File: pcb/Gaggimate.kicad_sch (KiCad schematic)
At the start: 66 parts, among them J1 USB_C_Receptacle, J10 Conn_01x02, J2 Conn_01x02, J3 Conn_01x03, J4 Conn_01x04, J5 Conn_01x04, J6 Conn_01x10, J7 Conn_01x02, J8 Conn_01x02, J9 Conn_01x04, K1 Relay_SPDT, K2 Relay_SPDT, K3 Relay_SPDT, Q1 MMBT2222A, Q2 MMBT2222A, Q3 MMBT2222A, SW1 SW_Push, SW2 SW_Push, U1 ESP32-S3-WROOM-1, U2 AMS1117-3.3, U3 USBLC6-2SC6, U6 MAX31855EASA

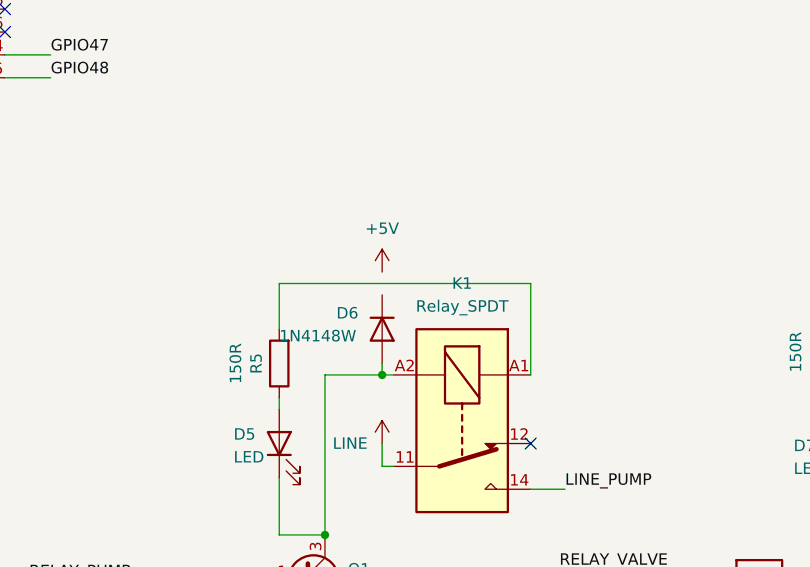
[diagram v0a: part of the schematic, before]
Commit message: feat: Add adjustments to PCB, pcb diff pipeline
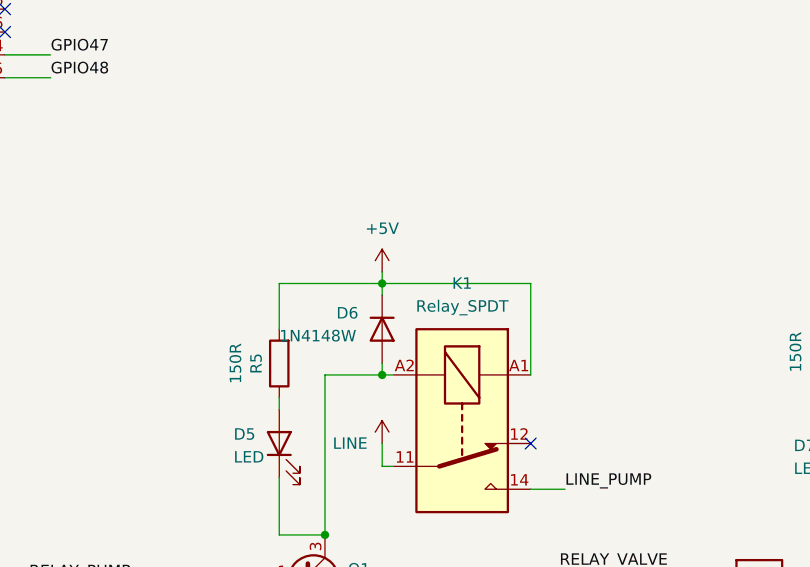
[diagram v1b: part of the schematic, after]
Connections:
- net +5V: now also D6.1 (K), K1.A1, R5.2
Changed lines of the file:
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@@
+	)
+	(junction
+		(at 240.03 135.89)
+		(diameter 0)
+		(color 0 0 0 0)
 	)
 	(junction
@@
 	(wire
 		(pts
+			(xy 240.03 134.62) (xy 240.03 135.89)
+		)
+		(stroke
+			(width 0)
+			(type default)
+		)
+	)
+	(wire
+		(pts
 			(xy 127.762 152.654) (xy 138.938 152.654)
 		)
@@
 	(wire
 		(pts
+			(xy 240.03 135.89) (xy 256.54 135.89)
+		)
+		(stroke
+			(width 0)
+			(type default)
+		)
+	)
+	(wire
+		(pts
 			(xy 358.14 92.71) (xy 361.95 92.71)
 		)
@@
 	(wire
 		(pts
-			(xy 228.6 135.89) (xy 256.54 135.89)
+			(xy 228.6 135.89) (xy 240.03 135.89)
 		)
 		(stroke
@@
 		)
 		(stroke
+			(width 0)
+			(type default)
+		)
+	)
+	(wire
+		(pts
+			(xy 240.03 135.89) (xy 240.03 137.16)
+		)
+		(stroke

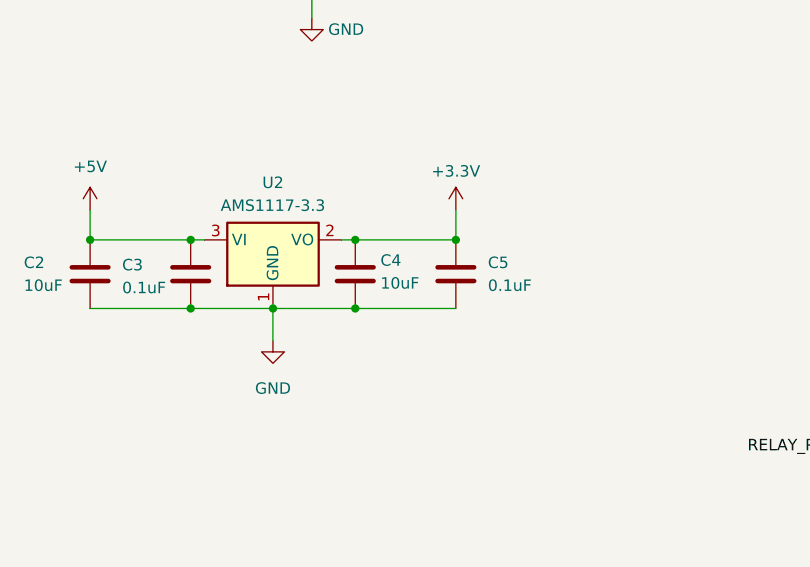
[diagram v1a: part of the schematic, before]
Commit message: feat: Replace 10uF output capacitor with 22uF
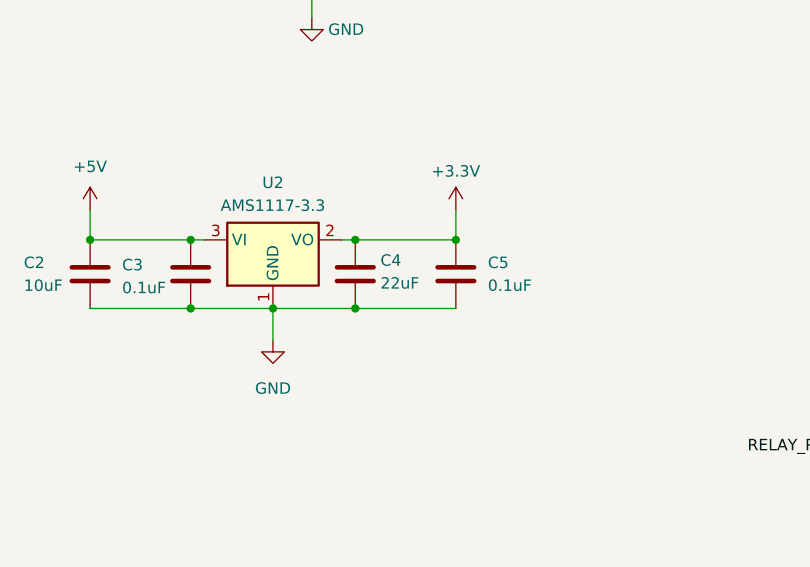
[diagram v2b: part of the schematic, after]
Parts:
- C4: value 10uF -> 22uF; LCSC C15850 -> C45783
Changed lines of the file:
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@@
 			)
 		)
-		(property "Value" "10uF"
+		(property "Value" "22uF"
 			(at 160.02 149.86 0)
 			(effects
@@
 			)
 		)
-		(property "LCSC" "C15850"
+		(property "LCSC" "C45783"
 			(at 160.02 147.32 0)
 			(effects

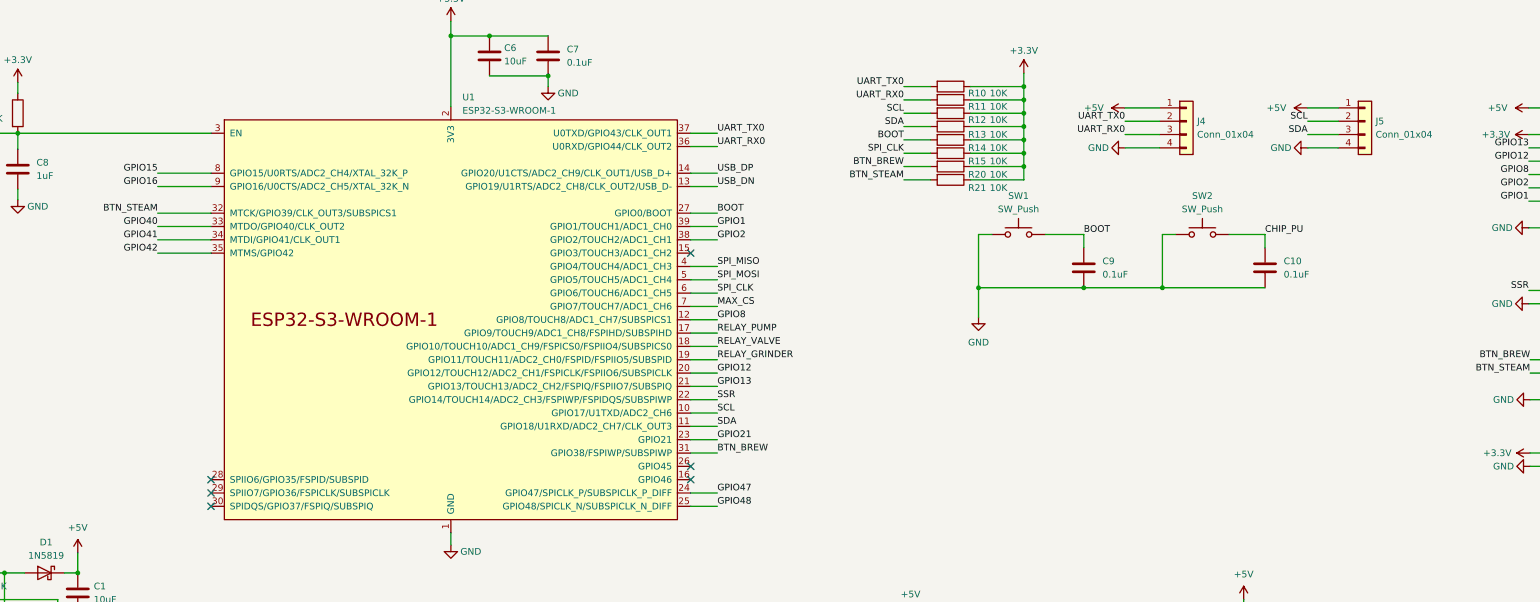
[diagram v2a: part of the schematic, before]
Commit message: feat: Move MAX31885, add SDA2, add silkscreen adjustments
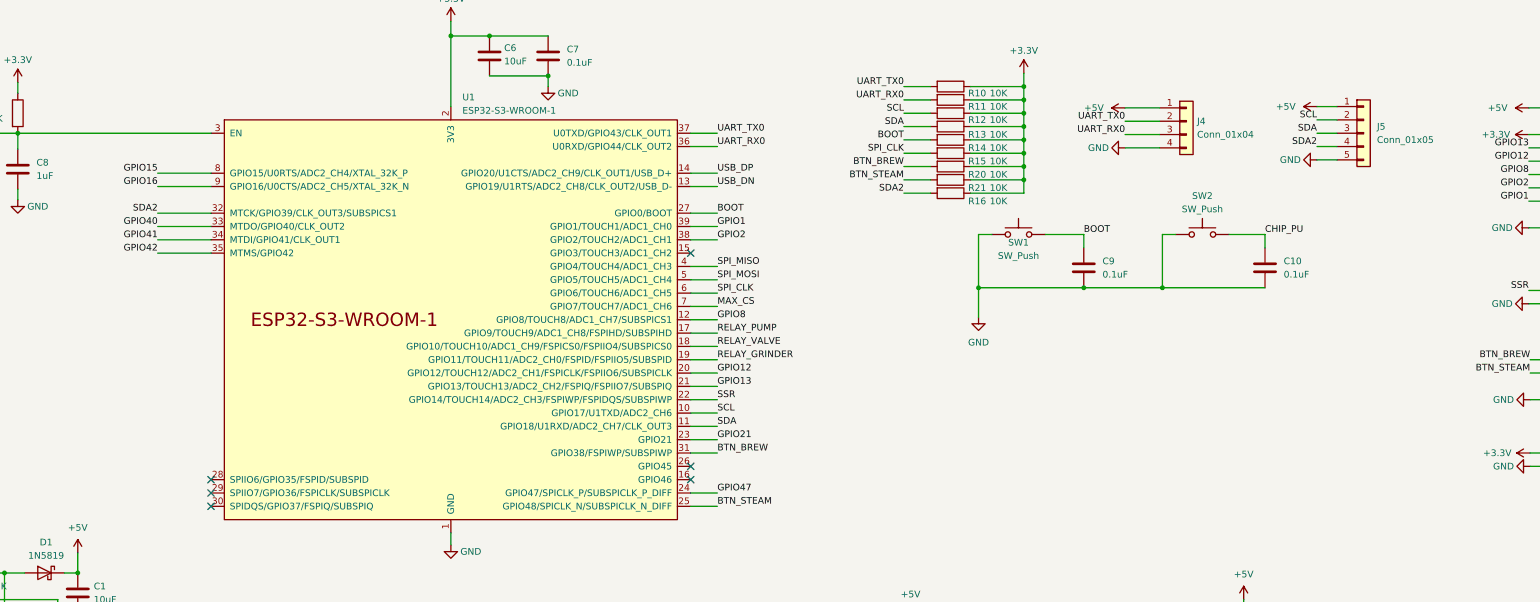
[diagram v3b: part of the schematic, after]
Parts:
- removed J5: Conn_01x04, Connector_JST:JST_XH_B4B-XH-A_1x04_P2.50mm_Vertical, symbol Connector_Generic:Conn_01x04
- added J5: Conn_01x05, Connector_JST:JST_XH_B5B-XH-A_1x05_P2.50mm_Vertical, symbol Connector_Generic:Conn_01x05
- added R16: 10K, Resistor_SMD:R_0805_2012Metric, symbol Device:R
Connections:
- net GPIO48 is gone; now on net BTN_STEAM: U1.25 (GPIO48/SPICLK_N/SUBSPICLK_N_DIFF)
- net +3.3V: now also R16.1
- net +5V: now also J5.1 (Pin_1)
- net BTN_STEAM: no longer U1.32 (MTCK/GPIO39/CLK_OUT3/SUBSPICS1)
- net GND: now also J5.5 (Pin_5)
- net SCL: now also J5.2 (Pin_2)
- net SDA: now also J5.3 (Pin_3)
- new net SDA2: J5.4 (Pin_4), R16.2, U1.32 (MTCK/GPIO39/CLK_OUT3/SUBSPICS1)

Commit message: fix: Exchange switch for correct model
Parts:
- H1: now left out of the parts list
- SW1, SW2: LCSC C2909692 -> C116647
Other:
- title: (none) -> GaggiMate Controller PCB
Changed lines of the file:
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@@
 	(generator_version "8.0")
 	(paper "A3")
+	(title_block
+		(title "GaggiMate Controller PCB")
+		(date "2024-11-24")
+		(rev "1.0")
+	)
 	(junction
 		(at 361.95 92.71)
@@
 			)
 		)
-		(property "LCSC" "C2909692"
+		(property "LCSC" "C116647"
 			(at 260.604 53.848 0)
 			(effects
@@
 			)
 		)
-		(property "LCSC" "C2909692"
+		(property "LCSC" "C116647"
 			(at 295.656 53.848 0)
 			(effects
@@
 		(unit 1)
 		(exclude_from_sim no)
-		(in_bom yes)
+		(in_bom no)
 		(on_board yes)
 		(dnp no)

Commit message: fix: Move back connectors to allow expansion to fit
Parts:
- J9: LCSC (none) -> C144395
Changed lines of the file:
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@@
+			)
+		)
+		(property "LCSC" "C144395"
+			(at 369.062 87.63 0)
+			(effects
+				(font
+					(size 1.27 1.27)
+				)
+				(hide yes)
 			)
 		)
